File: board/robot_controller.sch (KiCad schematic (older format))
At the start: 57 parts, among them U2 STM32F405-144

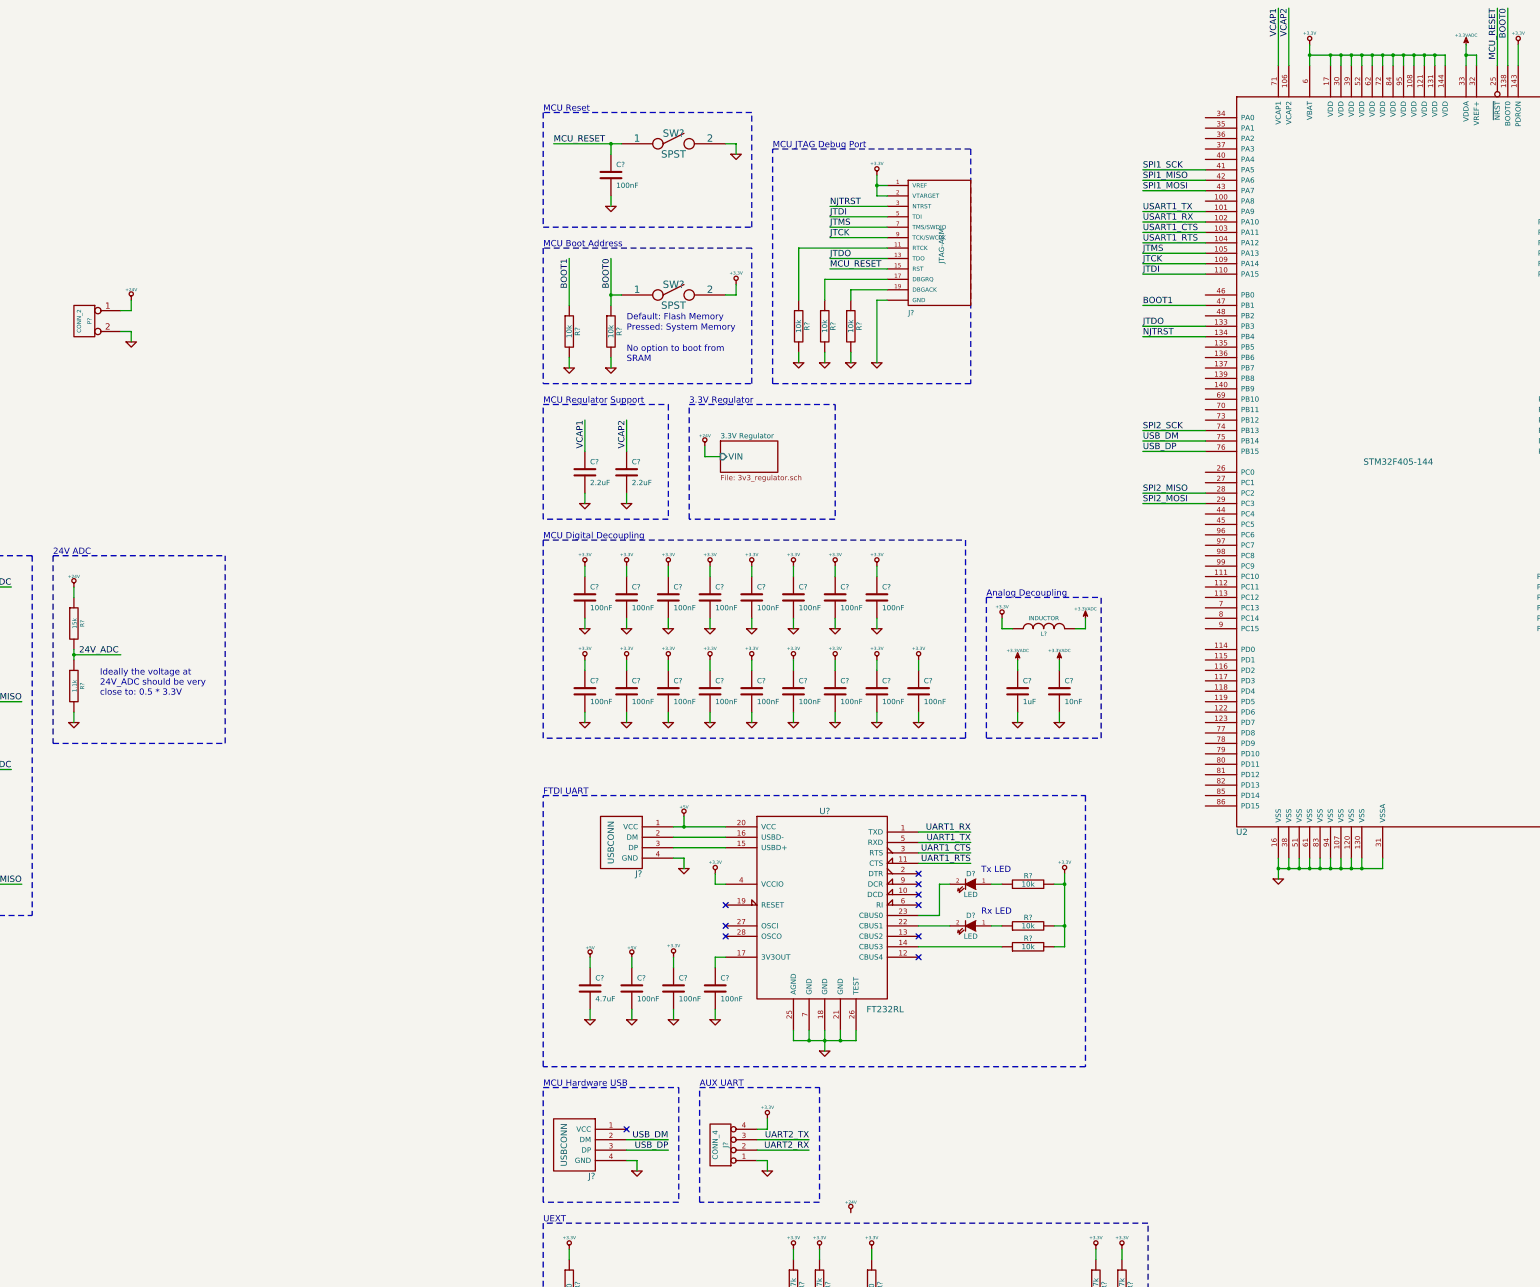
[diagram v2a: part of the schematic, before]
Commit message: Connected USB VBUS to the right MCU pin.
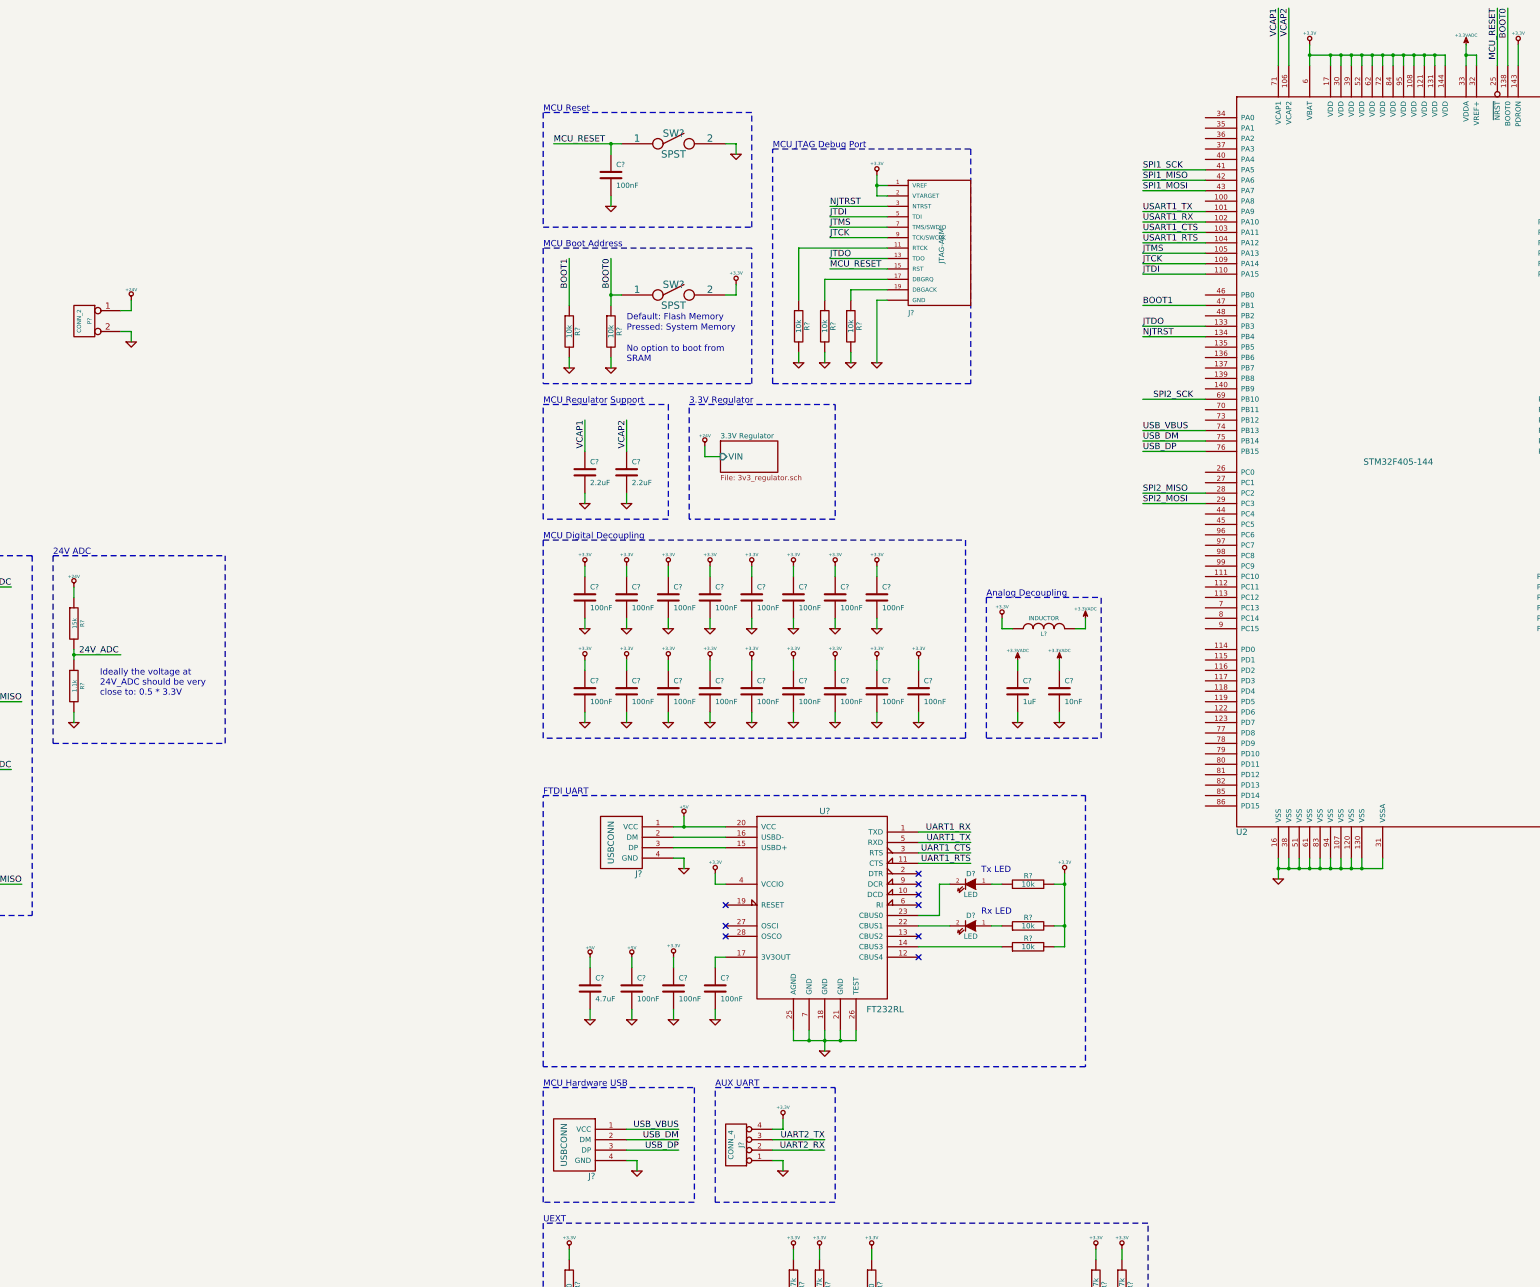
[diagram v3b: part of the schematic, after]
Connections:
- net SPI2_SCK: now also U2.69 (PB10); no longer U2.74 (PB13)
- net USB_VBUS: now reaches J?.1 (VCC)
- net USB_VBUS: now also U2.74 (PB13)
- no-connect marks 14 -> 13
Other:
- moved on the sheet: J?
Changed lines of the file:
@@
 	1    0    0    -1
 $EndComp
-NoConn ~ 30450 23550
-Text Label 30850 23650 2    60   ~ 0
+Text Label 30950 23650 2    60   ~ 0
 USB_DM
-Text Label 30850 23750 2    60   ~ 0
+Text Label 30950 23750 2    60   ~ 0
 USB_DP
 NoConn ~ 31400 21400
@@
 Text Label 35400 17450 0    60   ~ 0
 SPI2_MISO
-Text Label 35400 16850 0    60   ~ 0
+Text Label 35500 16550 0    60   ~ 0
 SPI2_SCK
 Text Notes 19000 15000 0    60   ~ 0
@@
 L CONN_4 J?
 U 1 1 52F1CD26
-P 31350 23700
-F 0 "J?" V 31300 23700 50  0000 C CNN
-F 1 "CONN_4" V 31400 23700 50  0000 C CNN
-F 2 "" H 31350 23700 60  0000 C CNN
-F 3 "" H 31350 23700 60  0000 C CNN
-	1    31350 23700
+P 31500 23700
+F 0 "J?" V 31450 23700 50  0000 C CNN
+F 1 "CONN_4" V 31550 23700 50  0000 C CNN
+F 2 "" H 31500 23700 60  0000 C CNN
+F 3 "" H 31500 23700 60  0000 C CNN
+	1    31500 23700
 	-1   0    0    1
 $EndComp
@@
 L +3.3V #PWR?
 U 1 1 52F1DA8C
-P 31800 23450
-F 0 "#PWR?" H 31800 23410 30  0001 C CNN
-F 1 "+3.3V" H 31800 23560 30  0000 C CNN
-F 2 "" H 31800 23450 60  0000 C CNN
-F 3 "" H 31800 23450 60  0000 C CNN
-	1    31800 23450
+P 31950 23450
+F 0 "#PWR?" H 31950 23410 30  0001 C CNN
+F 1 "+3.3V" H 31950 23560 30  0000 C CNN
+F 2 "" H 31950 23450 60  0000 C CNN
+F 3 "" H 31950 23450 60  0000 C CNN
+	1    31950 23450
 	1    0    0    -1
 $EndComp
@@
 L GND #PWR?
 U 1 1 52F1DD1F
-P 31800 23950
-F 0 "#PWR?" H 31800 23950 30  0001 C CNN
-F 1 "GND" H 31800 23880 30  0001 C CNN
-F 2 "" H 31800 23950 60  0000 C CNN
-F 3 "" H 31800 23950 60  0000 C CNN
-	1    31800 23950
-	1    0    0    -1
-$EndComp
-Text Label 32200 23750 2    60   ~ 0
+P 31950 23950
+F 0 "#PWR?" H 31950 23950 30  0001 C CNN
+F 1 "GND" H 31950 23880 30  0001 C CNN
+F 2 "" H 31950 23950 60  0000 C CNN
+F 3 "" H 31950 23950 60  0000 C CNN
+	1    31950 23950
+	1    0    0    -1
+$EndComp
+Text Label 32350 23750 2    60   ~ 0
 UART2_RX
-Text Label 32200 23650 2    60   ~ 0
+Text Label 32350 23650 2    60   ~ 0
 UART2_TX
-Text Notes 31150 23150 0    60   ~ 0
+Text Notes 31300 23150 0    60   ~ 0
 AUX UART
 Text Label 31850 25400 2    60   ~ 0
@@
 	38800 12800 38800 13350
 Wire Wire Line
-	29750 14100 30300 14100
-Wire Wire Line
-	30300 14100 30400 14100
+	29750 14100 30400 14100
 Wire Wire Line
 	30300 14600 30300 14700
@@
 	31500 14100 31500 14200
 Wire Wire Line
-	37000 13150 37000 13250
-Wire Wire Line
-	37000 13250 37000 13350
+	37000 13150 37000 13350
 Wire Wire Line
 	38600 13250 38600 13350
@@
 Connection ~ 37200 13250
 Wire Wire Line
-	38500 13150 38500 13250
-Wire Wire Line
-	38500 13250 38500 13350
+	38500 13150 38500 13350
 Connection ~ 38500 13250
 Wire Wire Line
@@
 	25150 18350 25150 18450
 Wire Wire Line
-	25150 18950 25150 19000
-Wire Wire Line
-	25150 19000 25150 19050
+	25150 18950 25150 19050
 Wire Wire Line
 	25150 19550 25150 19650
@@
 	36800 20950 36800 21050
 Wire Wire Line
-	36700 20950 36700 21050
-Wire Wire Line
-	36700 21050 36700 21150
-Wire Wire Line
-	36700 21050 36800 21050
-Wire Wire Line
-	36800 21050 36900 21050
-Wire Wire Line
-	36900 21050 37000 21050
-Wire Wire Line
-	37000 21050 37100 21050
-Wire Wire Line
-	37100 21050 37200 21050
-Wire Wire Line
-	37200 21050 37300 21050
-Wire Wire Line
-	37300 21050 37400 21050
-Wire Wire Line
-	37400 21050 37500 21050
-Wire Wire Line
-	37500 21050 37700 21050
+	36700 20950 36700 21150
+Wire Wire Line
+	36700 21050 37700 21050
 Connection ~ 36700 21050
 Connection ~ 36800 21050
@@
 	29900 15200 29900 15650
 Wire Wire Line
-	30300 15200 30300 15550
-Wire Wire Line
-	30300 15550 30300 15650
+	30300 15200 30300 15650
 Wire Wire Line
 	29900 16150 29900 16250
@@
 	31300 21900 31300 22000
 Wire Wire Line
-	34650 21100 34650 21200
-Wire Wire Line
-	34650 21200 34650 21600
-Wire Wire Line
-	34650 21600 34650 21800
+	34650 21100 34650 21800
 Wire Wire Line
 	33250 20900 33750 20900
@@
 	31300 21200 31400 21200
 Wire Wire Line
-	32050 22700 32200 22700
-Wire Wire Line
-	32200 22700 32350 22700
-Wire Wire Line
-	32350 22700 32500 22700
-Wire Wire Line
-	32500 22700 32650 22700
+	32050 22700 32650 22700
 Wire Wire Line
 	32650 22700 32650 22600
@@
 Connection ~ 32200 22700
 Wire Wire Line
-	32350 22600 32350 22700
-Wire Wire Line
-	32350 22700 32350 22800
+	32350 22600 32350 22800
 Connection ~ 32350 22700
 Wire Wire Line
@@
 Connection ~ 32500 22700
 Wire Wire Line
-	30900 20650 31000 20650
-Wire Wire Line
-	31000 20650 31400 20650
+	30900 20650 31400 20650
 Wire Wire Line
 	30900 20750 31400 20750
@@
 	36000 17050 35400 17050
 Wire Notes Line
-	29650 23150 30950 23150
-Wire Notes Line
-	30950 23150 30950 24250
-Wire Notes Line
-	30950 24250 29650 24250
+	29650 23150 31100 23150
+Wire Notes Line
+	31100 23150 31100 24250
+Wire Notes Line
+	31100 24250 29650 24250
 Wire Notes Line
 	29650 24250 29650 23150
@@
 	30450 23850 30550 23850
 Wire Wire Line
-	30450 23650 30850 23650
-Wire Wire Line
-	30450 23750 30850 23750
+	30450 23650 30950 23650
+Wire Wire Line
+	30450 23750 30950 23750
 Wire Wire Line
 	33450 21500 33250 21500
@@
 Wire Wire Line
 	36000 17450 35400 17450
-Wire Wire Line
-	36000 16850 35400 16850
 Wire Notes Line
 	19000 15000 20600 15000
@@
 	19000 16400 19000 15000
 Wire Wire Line
-	32850 14400 32850 14500
-Wire Wire Line
-	32850 14500 32850 14600
+	32850 14400 32850 14600
 Wire Wire Line
 	32850 14500 32950 14500
@@
 	29900 26300 30000 26300
 Wire Wire Line
-	31700 23850 31800 23850
-Wire Wire Line
-	31800 23850 31800 23950
-Wire Wire Line
-	31700 23550 31800 23550
-Wire Wire Line
-	31800 23550 31800 23450
-Wire Wire Line
-	32200 23650 31700 23650
-Wire Wire Line
-	32200 23750 31700 23750
-Wire Notes Line
-	31150 23150 32300 23150
-Wire Notes Line
-	32300 23150 32300 24250
-Wire Notes Line
-	32300 24250 31150 24250
-Wire Notes Line
-	31150 24250 31150 23150
+	31850 23850 31950 23850
+Wire Wire Line
+	31950 23850 31950 23950
+Wire Wire Line
+	31850 23550 31950 23550
+Wire Wire Line
+	31950 23550 31950 23450
+Wire Wire Line
+	32350 23650 31850 23650
+Wire Wire Line
+	32350 23750 31850 23750
+Wire Notes Line
+	31300 23150 32450 23150
+Wire Notes Line
+	32450 23150 32450 24250
+Wire Notes Line
+	32450 24250 31300 24250
+Wire Notes Line
+	31300 24250 31300 23150
 Wire Wire Line
 	31850 25500 31350 25500
@@
 $EndComp
 Wire Wire Line
-	37000 13250 37200 13250
-Wire Wire Line
-	37200 13250 37300 13250
-Wire Wire Line
-	37300 13250 37400 13250
-Wire Wire Line
-	37400 13250 37500 13250
-Wire Wire Line
-	37500 13250 37600 13250
-Wire Wire Line
-	37600 13250 37700 13250
-Wire Wire Line
-	37700 13250 37800 13250
-Wire Wire Line
-	37800 13250 37900 13250
-Wire Wire Line
-	37900 13250 38000 13250
-Wire Wire Line
-	38000 13250 38100 13250
-Wire Wire Line
-	38100 13250 38200 13250
-Wire Wire Line
-	38200 13250 38300 13250
+	37000 13250 38300 13250
 Wire Wire Line
 	38500 13250 38600 13250
@@
 Wire Notes Line
 	35000 19800 35000 18450
-$Comp
-L +24V #PWR?
-U 1 1 52F4FFAA
-P 32600 24350
-F 0 "#PWR?" H 32600 24300 20  0001 C CNN
-F 1 "+24V" H 32600 24450 30  0000 C CNN
-F 2 "" H 32600 24350 60  0000 C CNN
-F 3 "" H 32600 24350 60  0000 C CNN
-	1    32600 24350
-	1    0    0    -1
-$EndComp
 Wire Wire Line
 	31200 17000 31200 17100
@@
 Text Notes 25400 19400 0    60   ~ 0
 Ideally the voltage at\n24V_ADC should be very\nclose to: 0.5 * 3.3V
+Wire Wire Line
+	35400 16550 36000 16550
+Wire Wire Line
+	35400 16850 36000 16850
+Text Label 35400 16850 0    60   ~ 0
+USB_VBUS
+Wire Wire Line
+	30450 23550 30950 23550
+Text Label 30950 23550 2    60   ~ 0
+USB_VBUS
 $EndSCHEMATC
